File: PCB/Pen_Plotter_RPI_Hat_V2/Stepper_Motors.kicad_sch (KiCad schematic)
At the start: 14 parts, among them J2 X_LIMIT_SWITCH, J4 Y_LIMIT_SWITCH, J5 SERVO

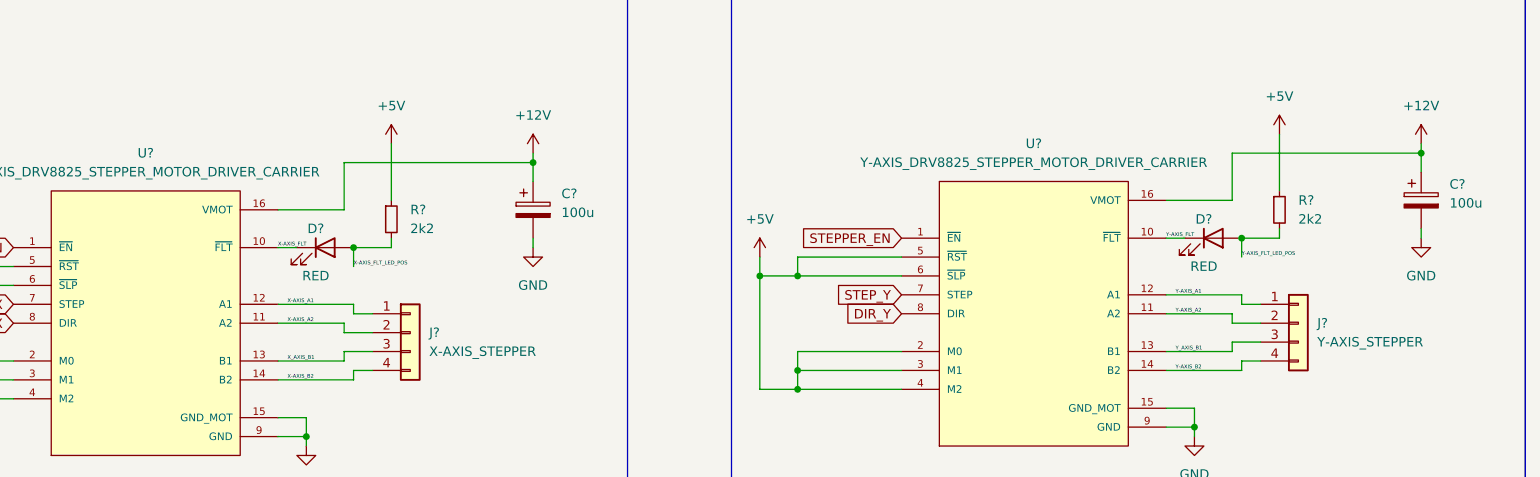
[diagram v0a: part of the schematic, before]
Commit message: Simplified design, began layout process
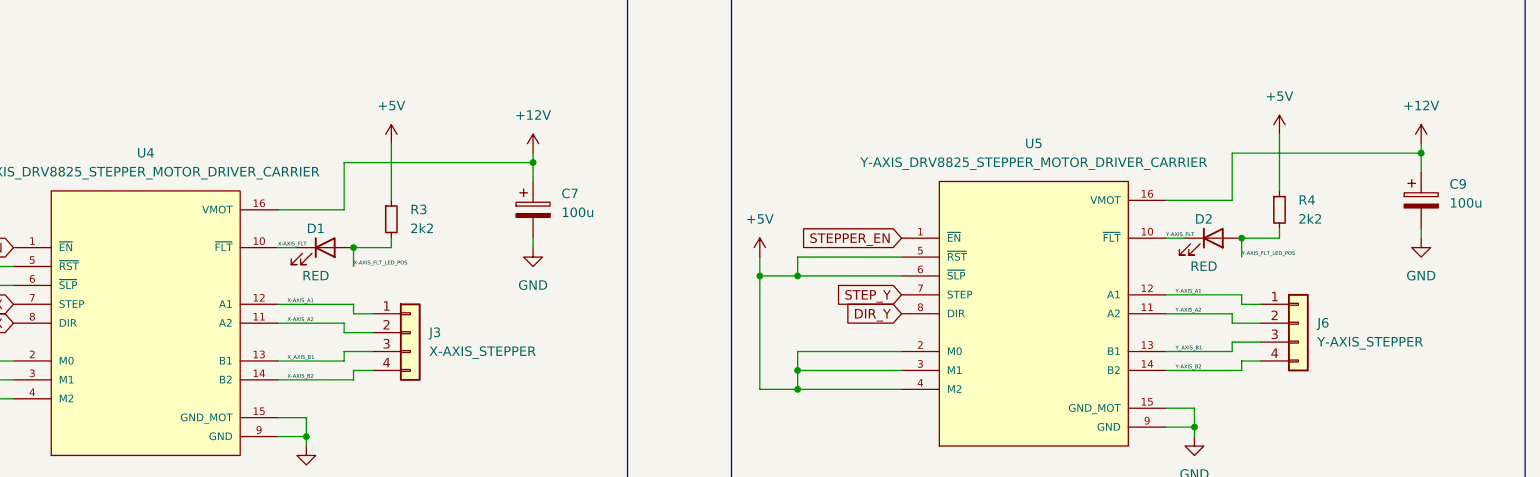
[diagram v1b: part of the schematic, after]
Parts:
- C7, C9: renamed from C?; footprint Capacitor_SMD:C_1206_3216Metric -> Capacitor_THT:CP_Radial_D8.0mm_P2.50mm
- C8: footprint Capacitor_SMD:C_1206_3216Metric -> Capacitor_THT:CP_Radial_D8.0mm_P2.50mm
- J2, J4: footprint (none) -> Connector_JST:JST_EH_B2B-EH-A_1x02_P2.50mm_Vertical
- J3, J6: renamed from J?; footprint (none) -> Connector_JST:JST_EH_B4B-EH-A_1x04_P2.50mm_Vertical
- J5: footprint (none) -> Connector_JST:JST_EH_B3B-EH-A_1x03_P2.50mm_Vertical
- gave numbers to parts that had none: 6

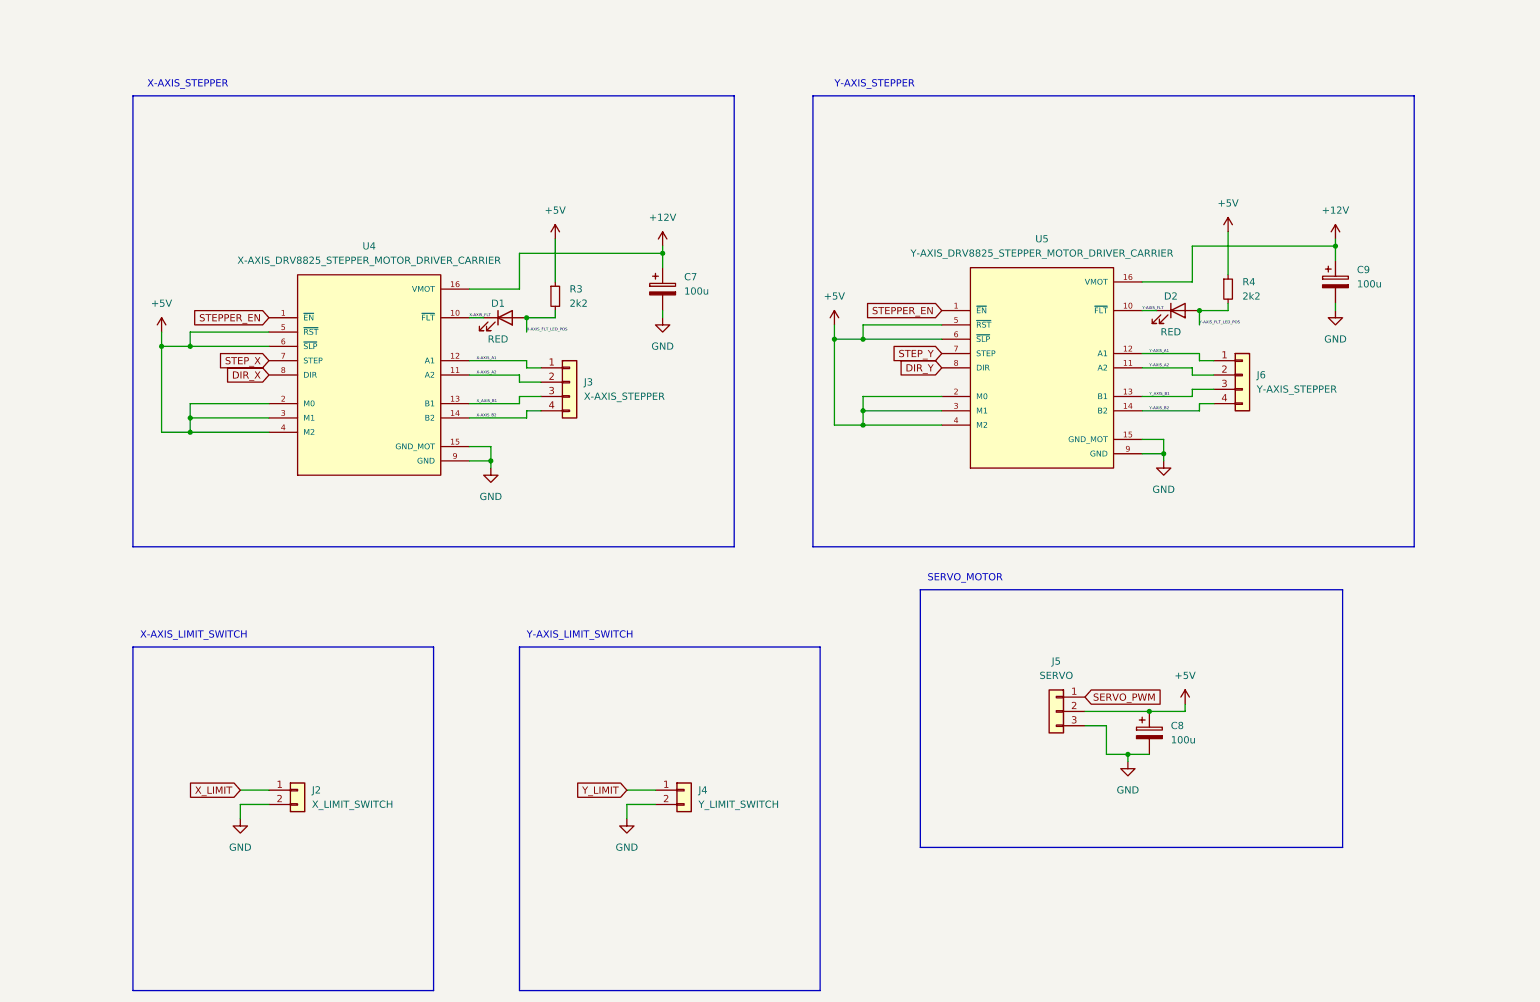
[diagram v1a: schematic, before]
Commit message: Added third stepper motor driver
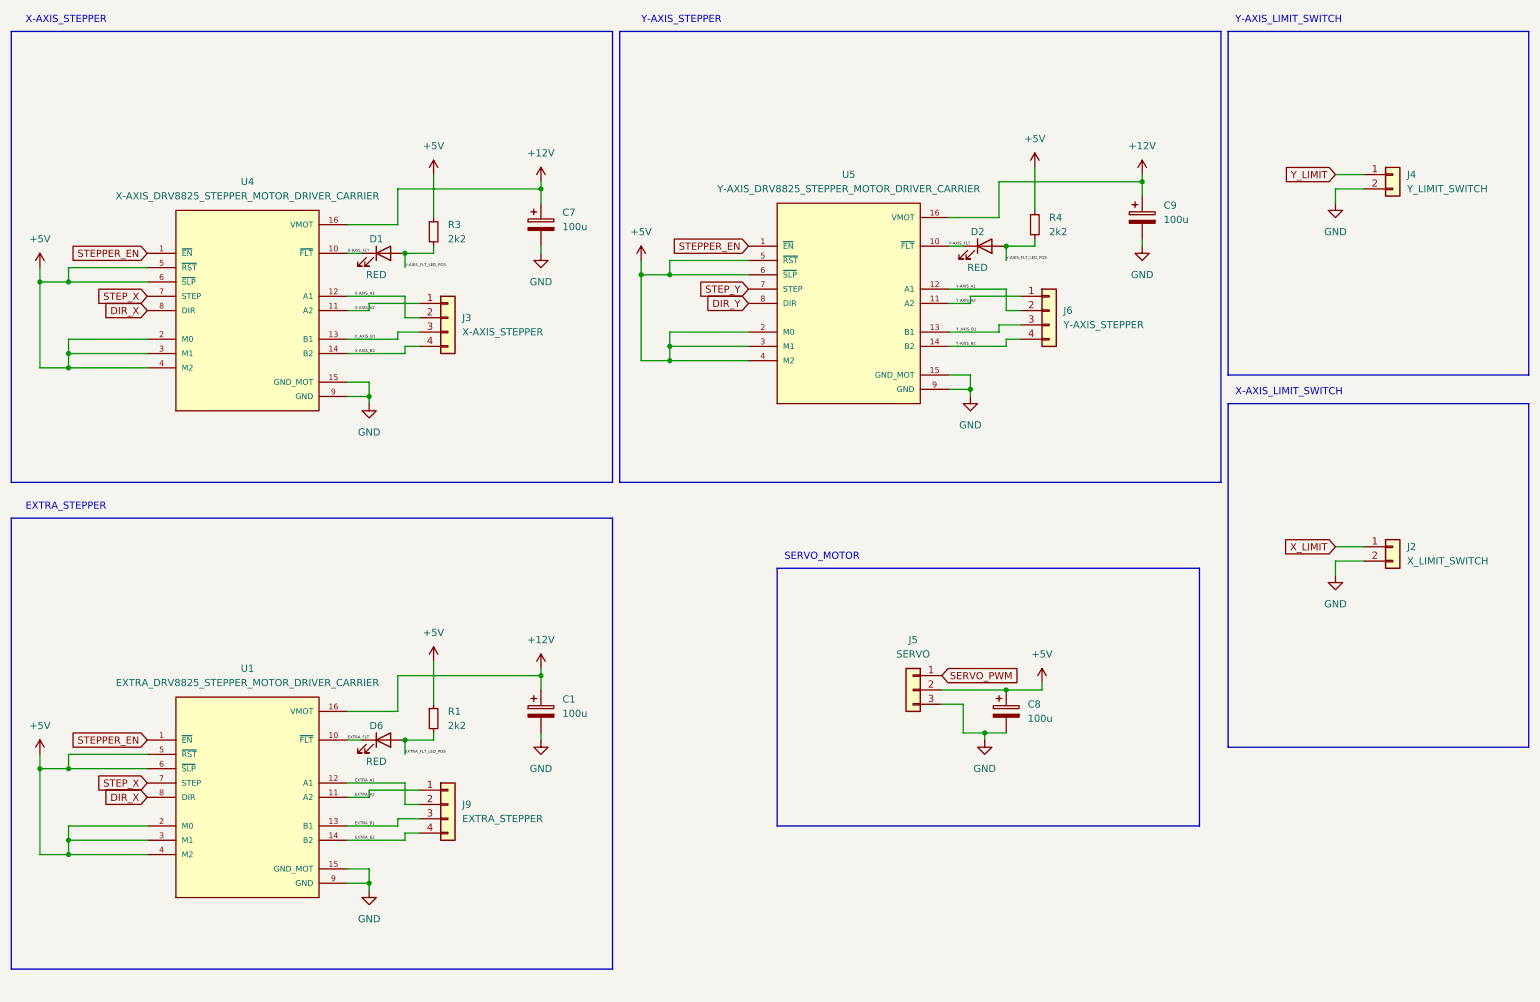
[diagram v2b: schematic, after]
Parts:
- added C1: 100u, Capacitor_THT:CP_Radial_D6.3mm_P2.50mm, symbol Device:C_Polarized
- added D6: RED, LED_THT:LED_D5.0mm, symbol Device:LED
- added J9: EXTRA_STEPPER, Connector_JST:JST_EH_B4B-EH-A_1x04_P2.50mm_Vertical, symbol Connector_Generic:Conn_01x04
- added R1: 2k2, Pen_Plotter_Lib:THT_RESISTOR_WITH_VALUE, symbol Device:R_Small
- added U1: EXTRA_DRV8825_STEPPER_MOTOR_DRIVER_CARRIER, Pen_Plotter_Lib:IC_DRV8825_STEPPER_MOTOR_DRIVER_CARRIER, symbol Pen_Plotter_Lib:DRV8825_STEPPER_MOTOR_DRIVER_CARRIER
- C7, C8, C9: footprint Capacitor_THT:CP_Radial_D8.0mm_P2.50mm -> Capacitor_THT:CP_Radial_D6.3mm_P2.50mm
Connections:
- net +12V: now also C1.1, U1.16 (VMOT)
- net +5V: now also R1.1, U1.2 (M0), U1.3 (M1), U1.4 (M2), U1.5 (~{RST}), U1.6 (~{SLP})
- net DIR_X: now also U1.8 (DIR)
- net GND: now also C1.2, U1.15 (GND_MOT), U1.9 (GND)
- net STEPPER_EN: now also U1.1 (~{EN})
- net STEP_X: now also U1.7 (STEP)
- net X-AXIS_A1: now also J3.2 (Pin_2); no longer J3.1 (Pin_1)
- net X-AXIS_A2: now also J3.1 (Pin_1); no longer J3.2 (Pin_2)
- net Y-AXIS_A1: now also J6.2 (Pin_2); no longer J6.1 (Pin_1)
- net Y-AXIS_A2: now also J6.1 (Pin_1); no longer J6.2 (Pin_2)
- new net EXTRA_A1: J9.2 (Pin_2), U1.12 (A1)
- new net EXTRA_A2: J9.1 (Pin_1), U1.11 (A2)
- new net EXTRA_B1: J9.3 (Pin_3), U1.13 (B1)
- new net EXTRA_B2: J9.4 (Pin_4), U1.14 (B2)
- new net EXTRA_FLT: D6.1 (K), U1.10 (~{FLT})
- new net EXTRA_FLT_LED_POS: D6.2 (A), R1.2
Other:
- note added: "EXTRA_STEPPER"
- moved on the sheet: C7, C8, C9, D1, D2, J2, J3, J4, J5, J6, R3, R4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
